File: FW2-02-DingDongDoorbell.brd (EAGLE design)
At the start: 62 x 37 mm, 12 parts, among them IC1 LM555N

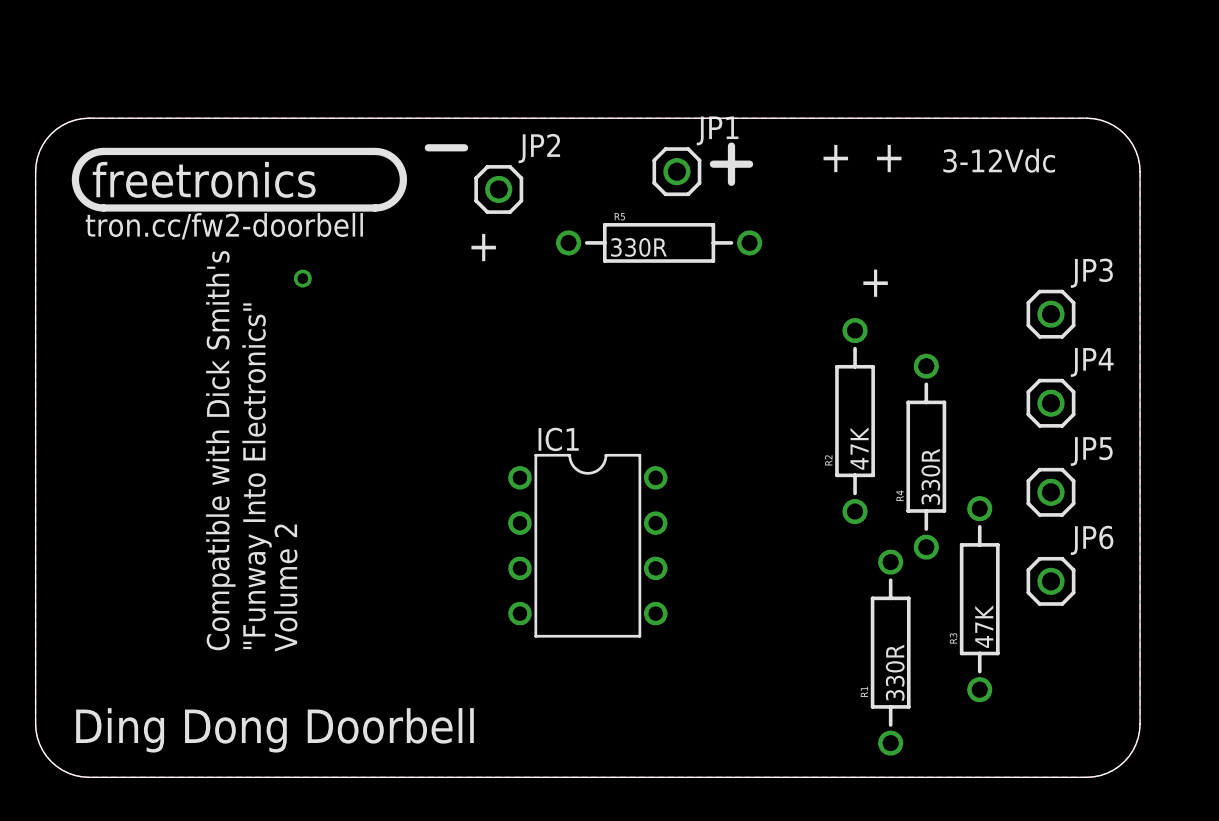
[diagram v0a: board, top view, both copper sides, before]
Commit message: Most of the schematic done, base part positions
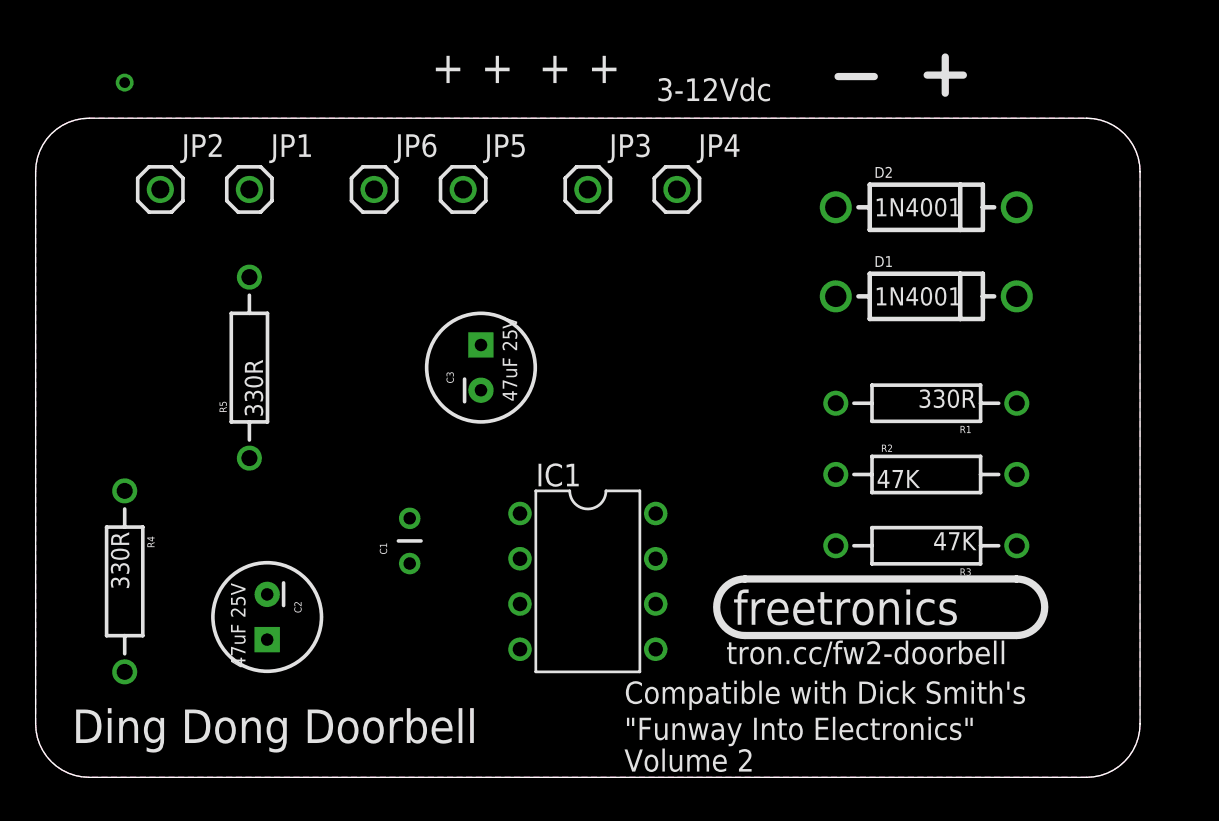
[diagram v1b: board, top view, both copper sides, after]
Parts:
- added C1: 100nF, freetronics-2:CAP-PTH-SMALL
- added C2, C3: 47uF 25V, freetronics-jon.1:CPOL-RADIAL-10UF-25V
- added D1, D2: 1N4001, freetronics-2:DIODE-1N4001
- JP5: value PWR- -> SPKR-
- JP6: value PWR- -> SPKR+
- moved R4 45.5 mm to (5.00, 11.0), turned to 270 degrees
- moved JP6 43.9 mm to (19.0, 33.0)
- moved JP5 37.1 mm to (24.0, 33.0)
- moved JP3 26.9 mm to (31.0, 33.0)
- moved JP4 24.2 mm to (36.0, 33.0)
- moved R5 24.0 mm to (12.0, 23.0), turned to 90 degrees
- moved JP1 24.0 mm to (12.0, 33.0)
- moved JP2 19.0 mm to (7.00, 33.0)
- moved R1 14.1 mm to (50.0, 21.0), turned to 180 degrees
- moved R2 5.00 mm to (50.0, 17.0), turned to 0 degrees
- moved R3 4.24 mm to (50.0, 13.0), turned to 180 degrees
- moved IC1 2.00 mm to (31.0, 11.0)
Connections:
- new net N$10: C1.2, C2.2, JP2.1, R4.P$1
- new net N$11: C1.1, R3.P$1
- new net N$3: D1.A, D2.A, JP4.1
- new net N$4: JP1.1, JP3.1, R1.P$2, R5.P$2
- new net N$5: JP6.1, R5.P$1
- new net N$6: C3.1, JP5.1
- new net N$7: C3.2
- new net N$8: C2.1, D2.C, R4.P$2
- net N$1: now also D1.C
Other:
- board text added: "SKU: FW2DOORBELL"
- board text removed: "SKU: FW2FLASH"

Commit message: Modified 555 symbol to match original; basic PCB routing
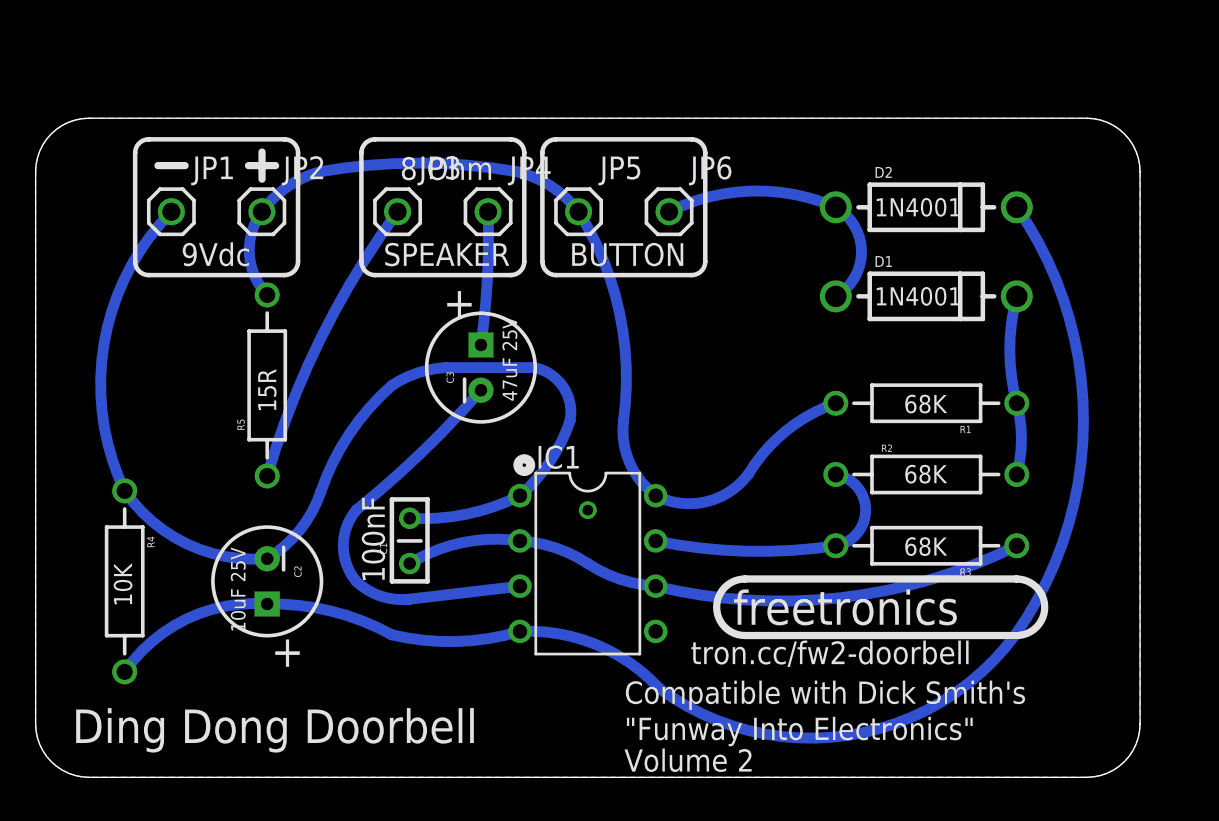
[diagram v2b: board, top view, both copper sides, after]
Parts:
- C2: value 47uF 25V -> 10uF 25V
- IC1: device linear:DIL08 -> freetronics-jon:DIL08
- JP1: value PWR+ -> PWR-
- JP2: value PWR- -> PWR+
- JP3: value PWR- -> SPKR+
- JP4: value PWR- -> SPKR-
- JP5: value SPKR- -> PWR-
- JP6: value SPKR+ -> PWR-
- R1: value 330R -> 68K
- R2, R3: value 47K -> 68K
- R4: value 330R -> 10K
- R5: value 330R -> 15R
- moved JP6 16.6 mm to (35.6, 31.8)
- moved JP3 10.8 mm to (20.3, 31.8)
- moved JP4 10.7 mm to (25.4, 31.8)
- moved JP5 6.60 mm to (30.5, 31.8)
- moved JP2 5.84 mm to (12.7, 31.8)
- moved JP1 4.55 mm to (7.62, 31.8)
- moved C2 2.00 mm to (13.0, 11.0)
- moved R5 1.41 mm to (13.0, 22.0)
- moved IC1 1.00 mm to (31.0, 12.0)
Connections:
- removed net GND: IC1.1
- removed net N$11: C1.1, R3.P$1
- removed net V+: IC1.8
- new net N$12: C1.1, IC1.2, IC1.6, R3.P$1
- net N$10: now also IC1.1, JP1.1; no longer JP2.1
- net N$2: now also IC1.7
- net N$3: now also JP6.1; no longer JP4.1
- net N$4: now also IC1.8, JP2.1, JP5.1; no longer JP1.1, JP3.1
- net N$5: now also JP3.1; no longer JP6.1
- net N$6: now also JP4.1; no longer JP5.1
- net N$7: now also IC1.3
- net N$8: now also IC1.4
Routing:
- net N$8: track 0.00 -> 75.9 mm
- net N$10: track 0.00 -> 59.9 mm
- net N$4: track 0.00 -> 52.1 mm
- net N$12: track 0.00 -> 34.7 mm
- net N$7: track 0.00 -> 23.1 mm
- net N$5: track 0.00 -> 16.5 mm
- net N$3: track 0.00 -> 14.4 mm
- net N$2: track 0.00 -> 14.1 mm
- net N$1: track 0.00 -> 10.0 mm
- net N$6: track 0.00 -> 7.49 mm
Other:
- board text added: "100nF"
- board text added: "8 Ohm"
- board text added: "9Vdc"
- board text added: "BUTTON"
- board text added: "SPEAKER"
- board text removed: "3-12Vdc"

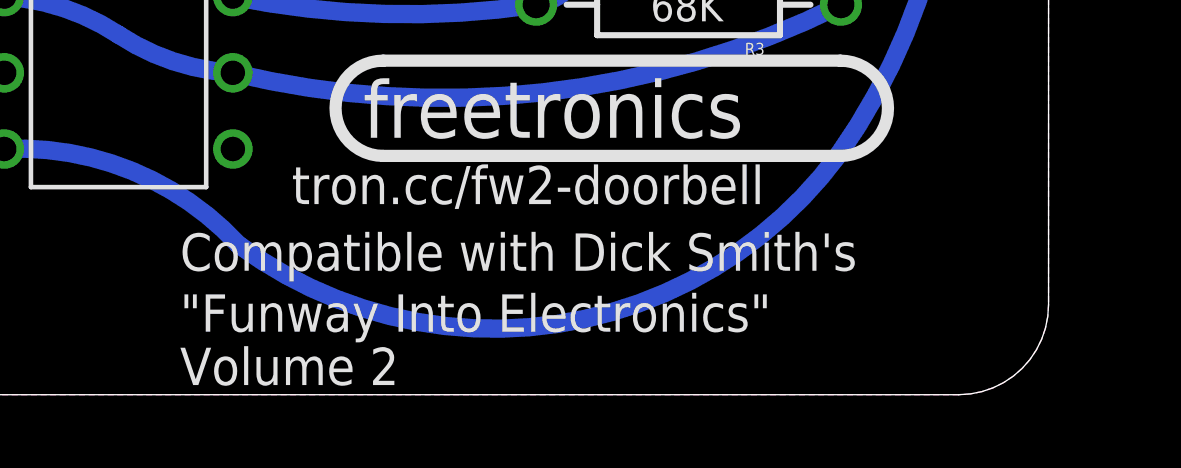
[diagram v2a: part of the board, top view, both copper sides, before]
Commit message: Updated silkscreen and labels
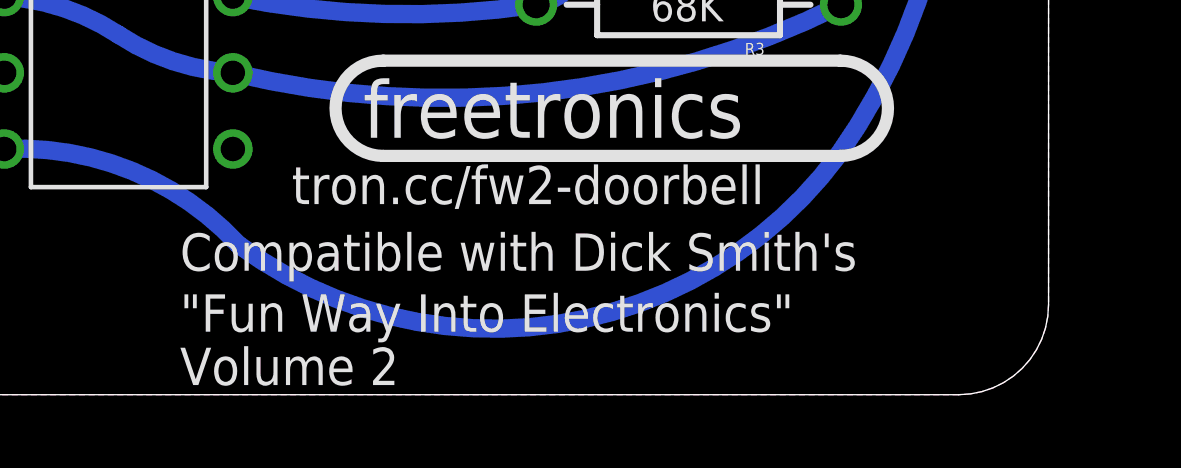
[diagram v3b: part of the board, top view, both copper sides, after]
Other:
- board text added: ""Fun Way Into Electronics""
- board text removed: ""Funway Into Electronics""
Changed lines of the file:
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@@
 <text x="59.35" y="1.082" size="1.27" layer="22" font="vector" ratio="16" rot="SMR0">SKU: FW2DOORBELL</text>
 <text x="33.048" y="4.132" size="1.2446" layer="21" font="vector" ratio="15">Compatible with Dick Smith's</text>
-<text x="33.048" y="2.1" size="1.2446" layer="21" font="vector" ratio="15">"Funway Into Electronics"</text>
+<text x="33.048" y="2.1" size="1.2446" layer="21" font="vector" ratio="15">"Fun Way Into Electronics"</text>
 <wire x1="11.948" y1="34.34" x2="13.472" y2="34.34" width="0.4064" layer="21"/>
 <wire x1="12.71" y1="35.102" x2="12.71" y2="33.578" width="0.4064" layer="21"/>

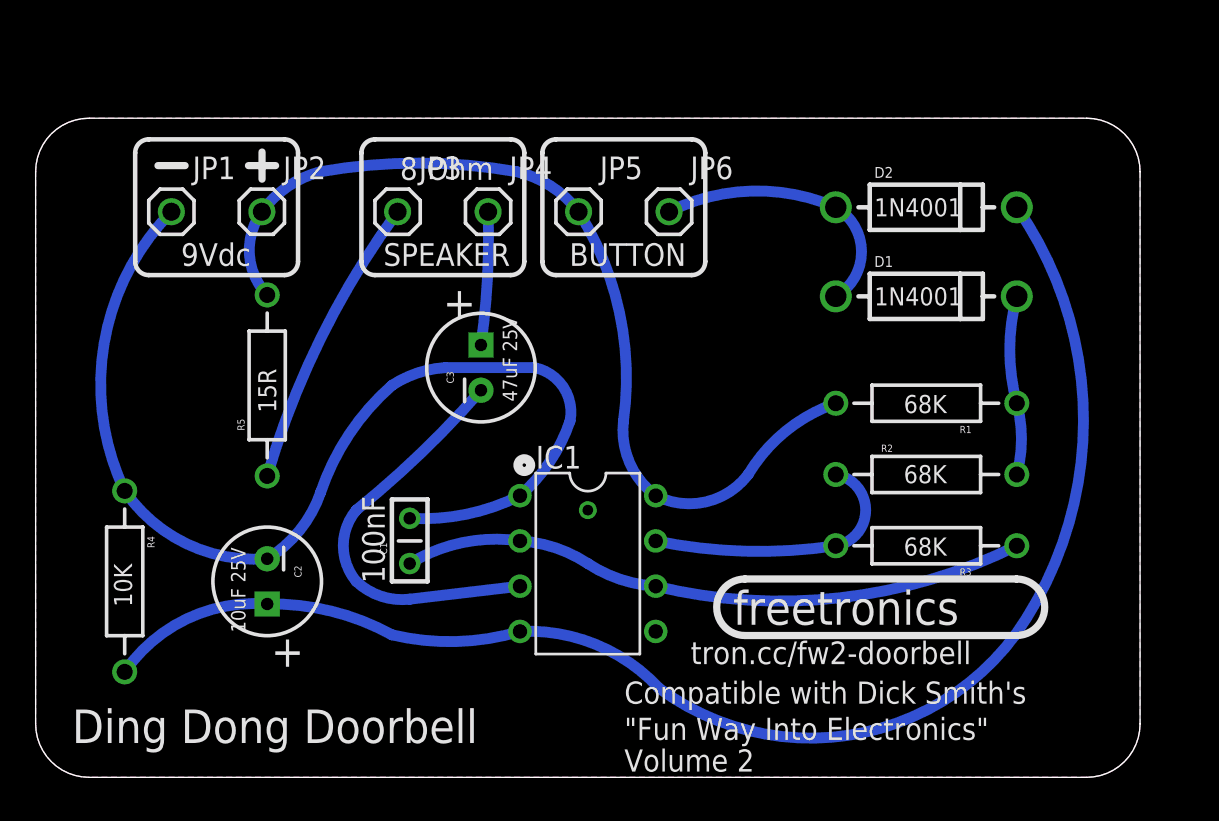
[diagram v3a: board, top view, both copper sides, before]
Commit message: Increased pad sizes; improved silkscreen
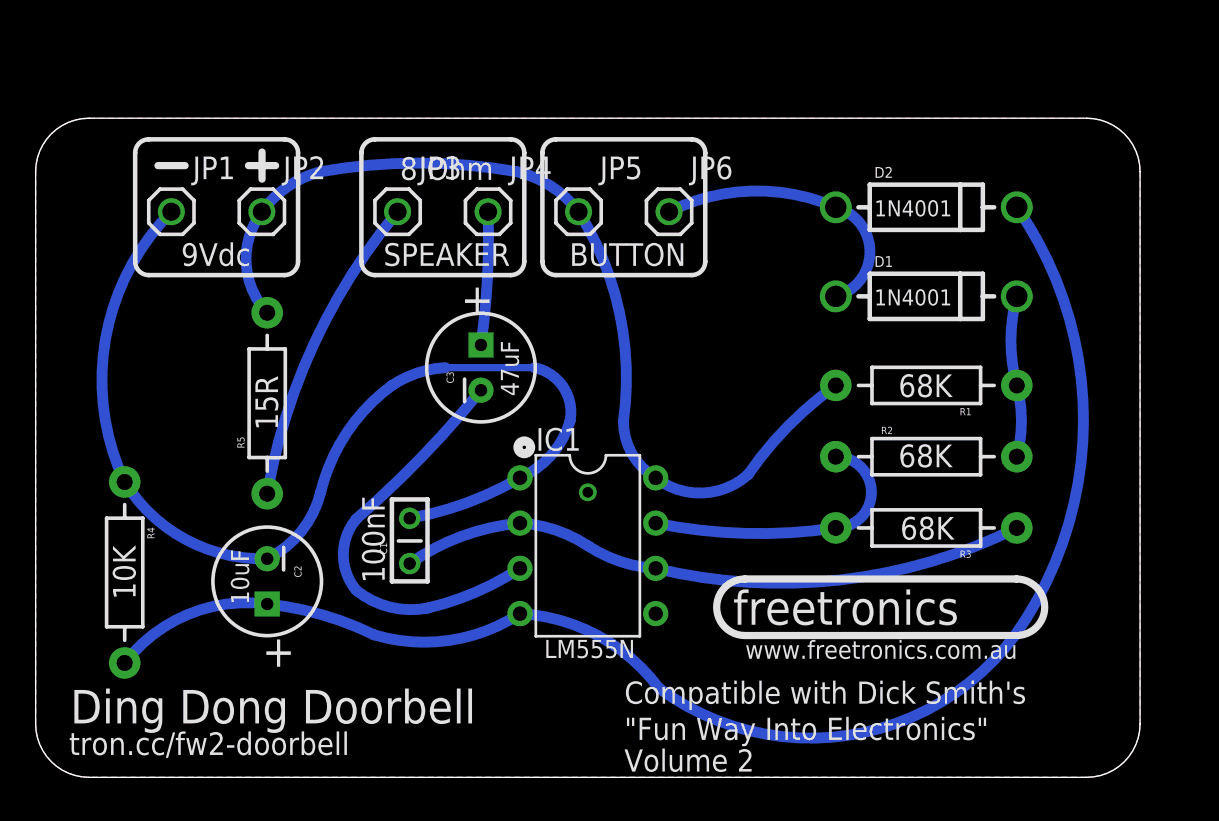
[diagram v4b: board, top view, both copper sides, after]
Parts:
- C2: value 10uF 25V -> 10uF
- C3: value 47uF 25V -> 47uF
- IC1: value LM555N -> 555L; device freetronics-jon:DIL08 -> freetronics-jon:DIL08L
- R1, R2, R3, R4, R5: device freetronics:FREETRONICS_AXIAL-0.4 -> freetronics:AXIAL-0.4-LARGE
- moved IC1 1.00 mm to (31.0, 13.0)
- moved R1 1.00 mm to (50.0, 22.0)
- moved R2 1.00 mm to (50.0, 18.0)
- moved R3 1.00 mm to (50.0, 14.0)
- moved R5 1.00 mm to (13.0, 21.0)
- moved R4 0.50 mm to (5.00, 11.5)
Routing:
- net N$1: track 10.0 -> 9.00 mm
- net N$5: track 16.5 -> 17.4 mm
- net N$10: track 59.9 -> 59.1 mm
- net N$7: track 23.1 -> 23.8 mm
- net N$4: track 52.1 -> 52.7 mm
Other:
- board text added: "LM555N"
- board text added: "v1.0"
- board text added: "www.freetronics.com.au"
